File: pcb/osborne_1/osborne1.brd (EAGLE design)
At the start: 40 x 97 mm, 20 parts, among them J2 ATX24RH

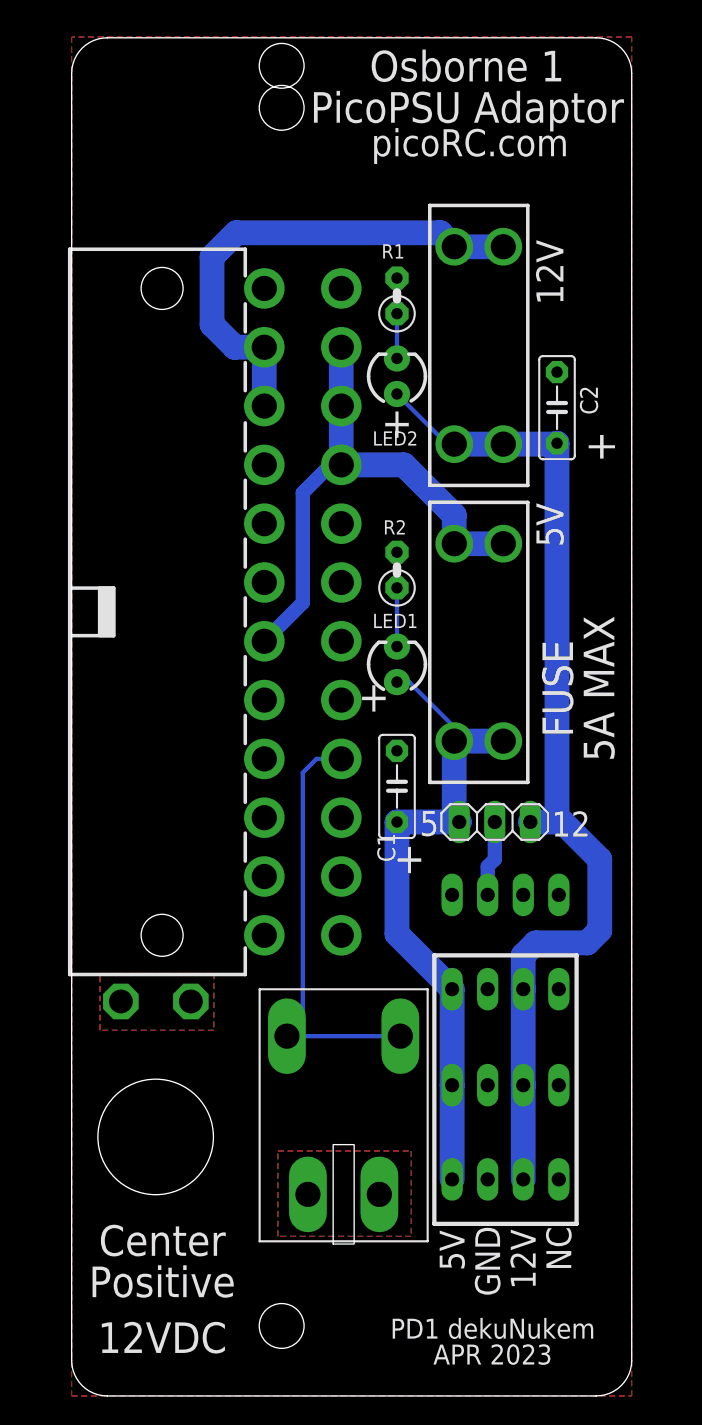
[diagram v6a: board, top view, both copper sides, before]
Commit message: correct orientation to allow grounding blade
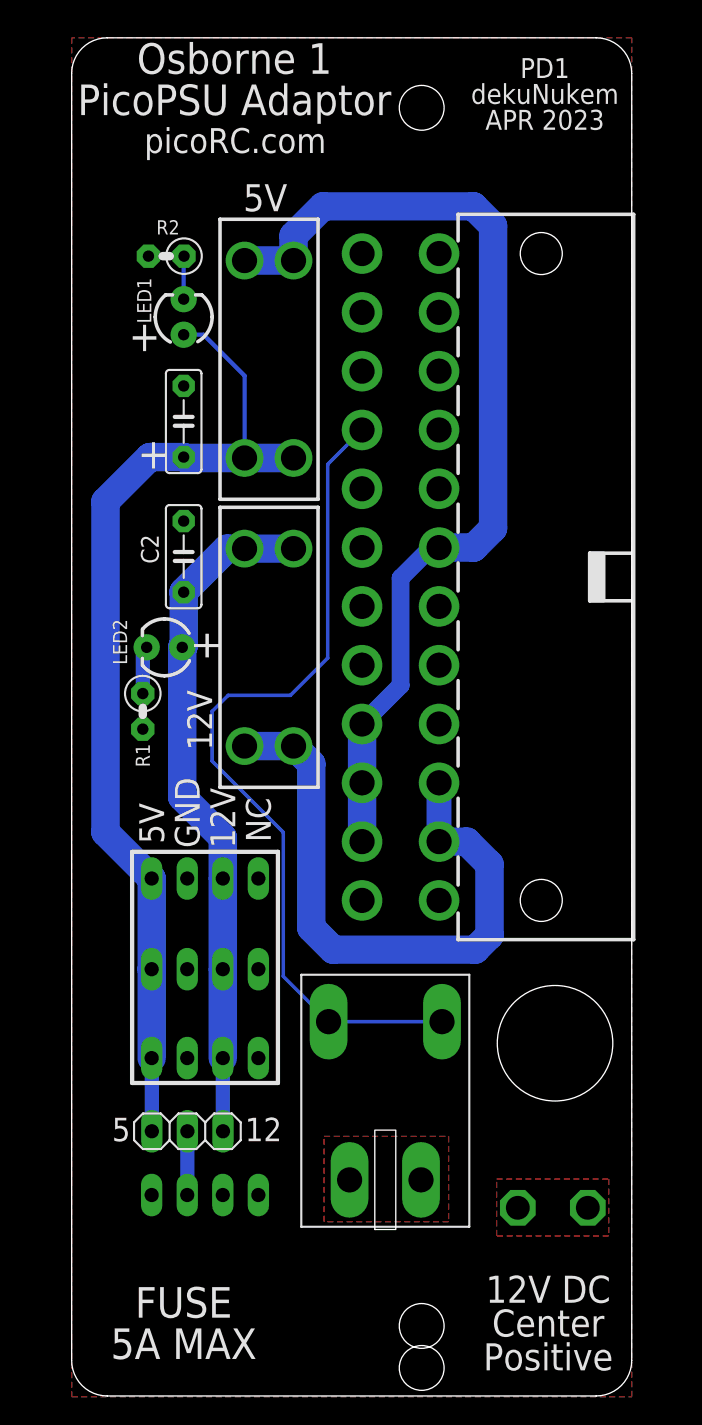
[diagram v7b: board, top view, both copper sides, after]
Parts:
- moved U$5 93.5 mm to (25.0, 2.00), turned to 0 degrees
- moved U$1 87.6 mm to (25.0, 92.0), turned to 0 degrees
- moved U$3 87.6 mm to (25.0, 5.00), turned to 0 degrees
- moved TP2 36.5 mm to (36.9, 13.4), turned to 90 degrees
- moved R1 34.8 mm to (5.08, 48.9), turned to 270 degrees
- moved JP4 31.1 mm to (8.27, 18.9)
- moved JP3 30.3 mm to (9.53, 14.4)
- moved C1 30.2 mm to (8.00, 69.6)
- moved LED1 29.1 mm to (8.00, 77.1)
- moved C2 28.7 mm to (8.00, 59.9)
- moved R2 27.8 mm to (6.75, 81.4), turned to 180 degrees
- moved TP1 27.6 mm to (31.9, 13.4), turned to 90 degrees
- moved U$2 26.3 mm to (14.1, 53.5), turned to 90 degrees
- moved LED2 25.5 mm to (6.63, 53.5), turned to 180 degrees
- moved U$8 25.2 mm to (14.1, 74.0)
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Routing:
- net N$6: track 38.8 -> 70.6 mm
- net N$1: track 30.6 -> 60.8 mm
- net +5V: track 47.5 -> 72.6 mm
- net +12V: track 73.3 -> 48.9 mm
- net N$8: track 35.4 -> 44.4 mm
- net N$3: track 4.19 -> 3.08 mm
- net N$2: track 5.42 -> 4.56 mm
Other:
- board text added: "12V DC Center Positive"
- board text added: "YELO"
- board text removed: "12VDC"
- board text removed: "Center Positive"
- board text removed: "PWR"
- board text removed: "YELLOW"

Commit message: minor cleanup
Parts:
- moved R1 0.89 mm to (5.08, 48.0)
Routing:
- net N$4: track 3.42 -> 4.31 mm
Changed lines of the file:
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@@
 <layer number="19" name="Unrouted" color="6" fill="1" visible="yes" active="yes"/>
 <layer number="20" name="Dimension" color="24" fill="1" visible="yes" active="yes"/>
-<layer number="21" name="tPlace" color="7" fill="1" visible="no" active="yes"/>
-<layer number="22" name="bPlace" color="7" fill="1" visible="no" active="yes"/>
+<layer number="21" name="tPlace" color="7" fill="1" visible="yes" active="yes"/>
+<layer number="22" name="bPlace" color="7" fill="1" visible="yes" active="yes"/>
 <layer number="23" name="tOrigins" color="15" fill="1" visible="yes" active="yes"/>
 <layer number="24" name="bOrigins" color="15" fill="1" visible="yes" active="yes"/>
-<layer number="25" name="tNames" color="7" fill="1" visible="no" active="yes"/>
-<layer number="26" name="bNames" color="7" fill="1" visible="no" active="yes"/>
-<layer number="27" name="tValues" color="7" fill="1" visible="no" active="yes"/>
-<layer number="28" name="bValues" color="7" fill="1" visible="no" active="yes"/>
+<layer number="25" name="tNames" color="7" fill="1" visible="yes" active="yes"/>
+<layer number="26" name="bNames" color="7" fill="1" visible="yes" active="yes"/>
+<layer number="27" name="tValues" color="7" fill="1" visible="yes" active="yes"/>
+<layer number="28" name="bValues" color="7" fill="1" visible="yes" active="yes"/>
 <layer number="29" name="tStop" color="7" fill="3" visible="no" active="yes"/>
 <layer number="30" name="bStop" color="7" fill="6" visible="no" active="yes"/>
@@
 <layer number="49" name="Reference" color="7" fill="1" visible="no" active="yes"/>
 <layer number="50" name="dxf" color="7" fill="1" visible="no" active="no"/>
-<layer number="51" name="tDocu" color="7" fill="1" visible="no" active="yes"/>
-<layer number="52" name="bDocu" color="7" fill="1" visible="no" active="yes"/>
+<layer number="51" name="tDocu" color="7" fill="1" visible="yes" active="yes"/>
+<layer number="52" name="bDocu" color="7" fill="1" visible="yes" active="yes"/>
 <layer number="53" name="tGND_GNDA" color="7" fill="1" visible="no" active="no"/>
 <layer number="54" name="bGND_GNDA" color="7" fill="1" visible="no" active="no"/>
@@
 <wire x1="14.732" y1="22.352" x2="4.318" y2="22.352" width="0.3048" layer="21"/>
 <wire x1="4.318" y1="22.352" x2="4.318" y2="38.862" width="0.3048" layer="21"/>
+<text x="5.334" y="57.15" size="2.1844" layer="25" distance="35" rot="R90" align="center">+</text>
 </plain>
 <attributes>
@@
 <attribute name="VALUE" x="6.628" y="55.753" size="0.6096" layer="27" font="vector" ratio="20" rot="R180" align="top-center"/>
 </element>
-<element name="R1" library="adafruit" package="0207/2V" value="" x="5.08" y="48.895" smashed="yes" rot="R270">
-<attribute name="NAME" x="5.588" y="44.9072" size="1.016" layer="25" ratio="10" rot="R90"/>
-<attribute name="VALUE" x="2.8448" y="48.9458" size="1.27" layer="27" ratio="10" rot="R270"/>
+<element name="R1" library="adafruit" package="0207/2V" value="" x="5.08" y="48.006" smashed="yes" rot="R270">
+<attribute name="NAME" x="3.429" y="47.7012" size="1.016" layer="25" ratio="10" rot="R90"/>
+<attribute name="VALUE" x="2.8448" y="48.0568" size="1.27" layer="27" ratio="10" rot="R270"/>
 </element>
 <element name="JP5" library="appleii" package="1X04" value="" x="9.525" y="36.957" smashed="yes" rot="MR180"/>
@@
 <contactref element="R1" pad="1"/>
 <wire x1="5.358" y1="53.467" x2="5.08" y2="53.189" width="1.016" layer="16"/>
-<wire x1="5.08" y1="53.189" x2="5.08" y2="50.165" width="1.016" layer="16"/>
+<wire x1="5.08" y1="53.189" x2="5.08" y2="49.276" width="1.016" layer="16"/>
 </signal>
 </signals>
